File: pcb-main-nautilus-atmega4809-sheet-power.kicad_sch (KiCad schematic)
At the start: 14 parts, among them U1 NCP1117-5.0_TO252, U2 AP2112K-3.3

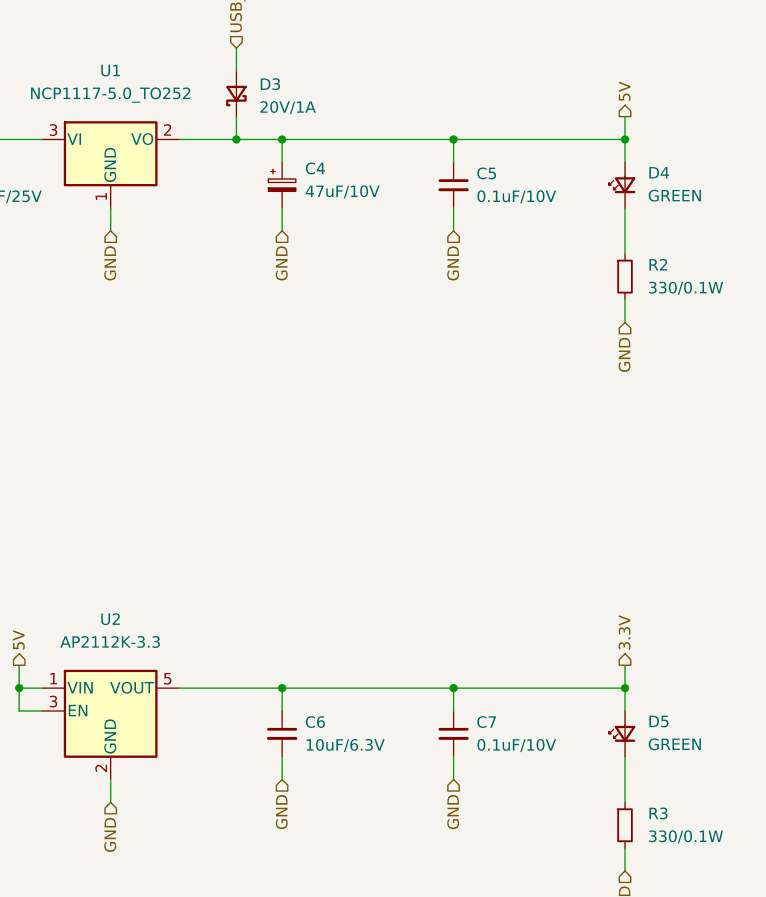
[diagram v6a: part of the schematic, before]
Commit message: Nest level shifter sheets under UPDI programmer and bridge sheet
Supports #2.
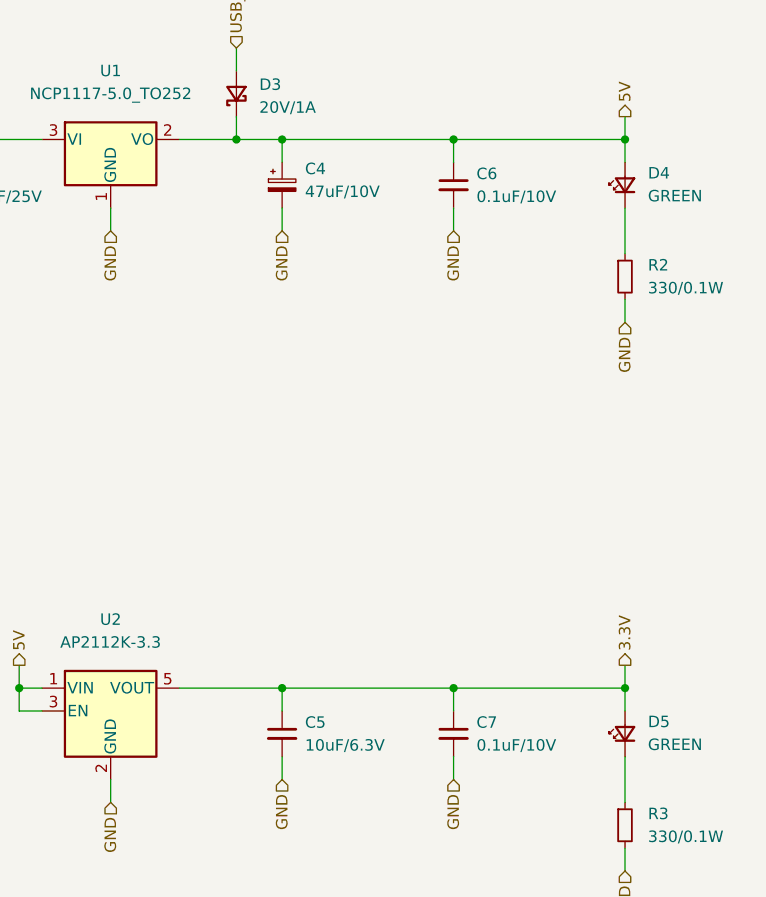
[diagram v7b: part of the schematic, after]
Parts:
- renumbered C6 to C5, C5 to C6
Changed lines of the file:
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@@
   (symbol (lib_id "Device:C_Small") (at 177.8 74.93 0) (unit 1)
     (in_bom yes) (on_board yes) (fields_autoplaced)
-    (property "Reference" "C5" (id 0) (at 180.34 73.6662 0)
+    (property "Reference" "C6" (id 0) (at 180.34 73.6662 0)
       (effects (font (size 1.27 1.27)) (justify left))
     )
@@
   (symbol (lib_id "Device:C_Small") (at 158.75 135.89 0) (unit 1)
     (in_bom yes) (on_board yes) (fields_autoplaced)
-    (property "Reference" "C6" (id 0) (at 161.29 134.6262 0)
+    (property "Reference" "C5" (id 0) (at 161.29 134.6262 0)
       (effects (font (size 1.27 1.27)) (justify left))
     )

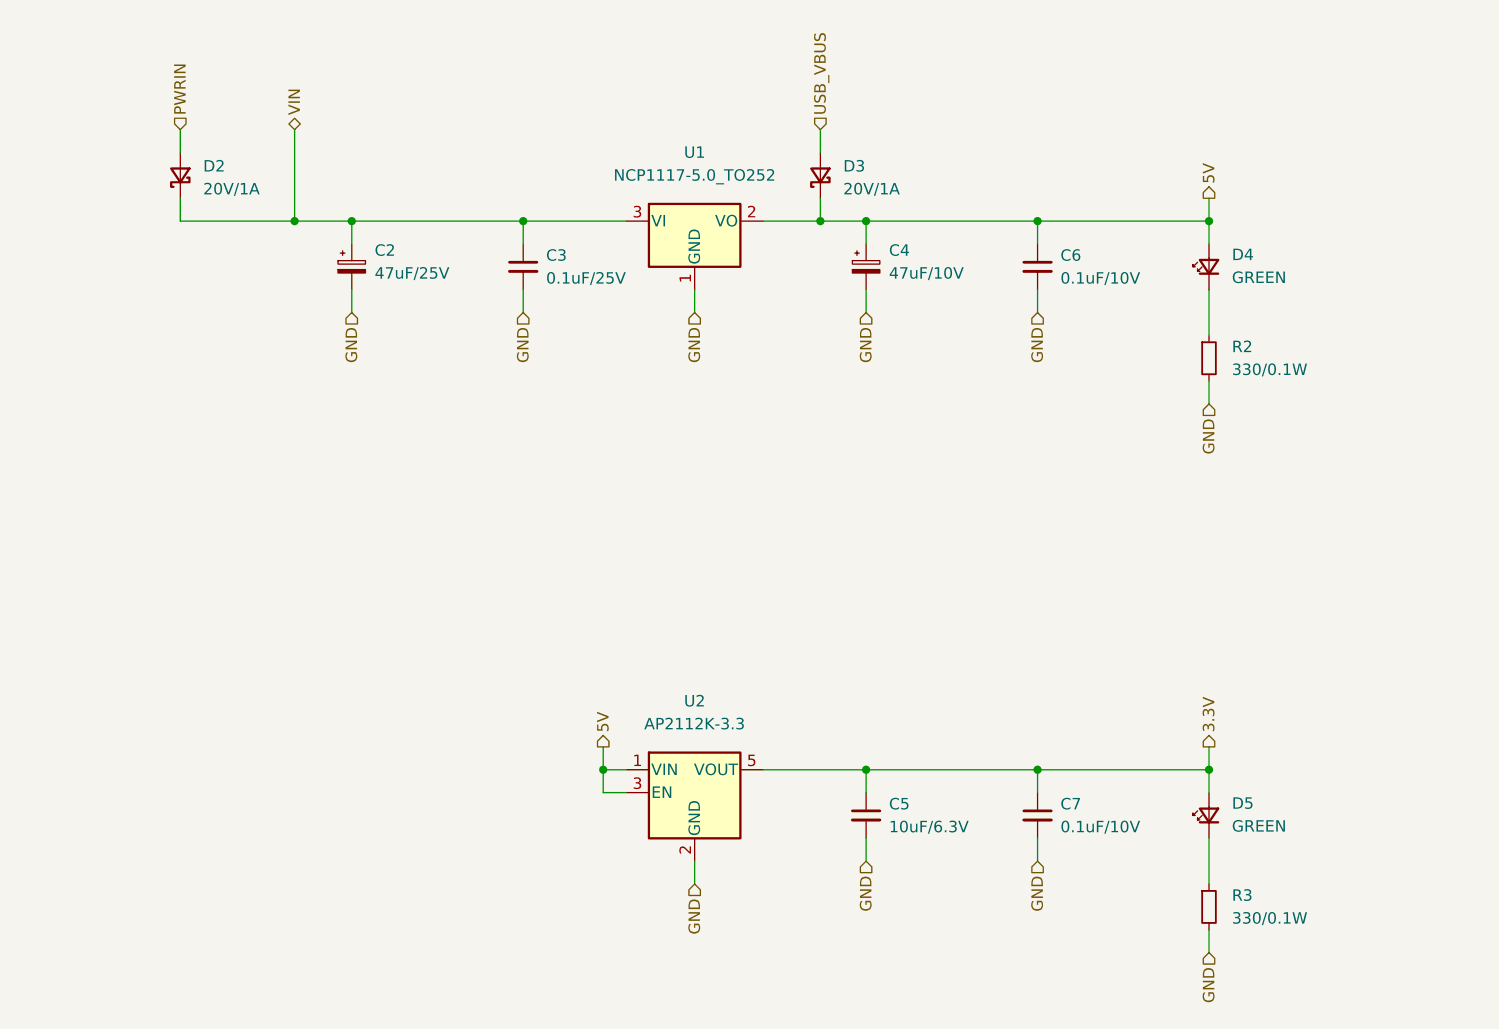
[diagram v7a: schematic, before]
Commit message: Serialize power sheet
Supports #2.
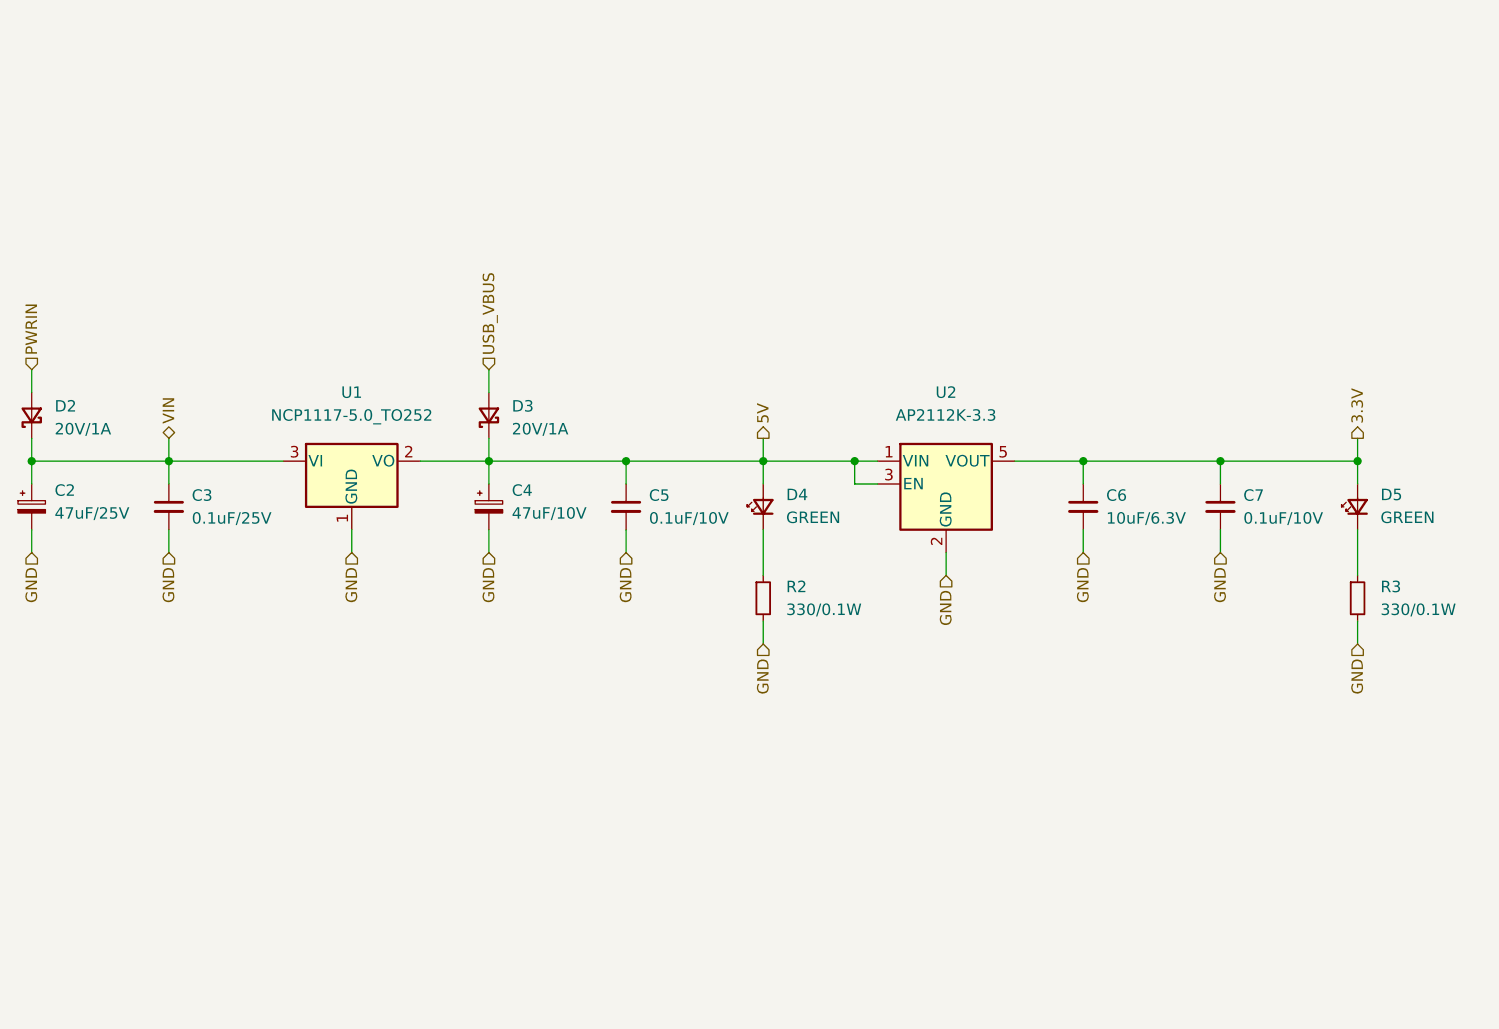
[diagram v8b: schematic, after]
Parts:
- renumbered C6 to C5, C5 to C6
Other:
- moved on the sheet: C2, C3, C4, C5, C6, C7, D2, D3, D4, D5, R2, R3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
